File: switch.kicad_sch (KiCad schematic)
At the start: 4 parts, among them U10 74LVC1G3157, U11 74LVC1G3157, U12 74LVC1G3157, U9 74LVC1G3157

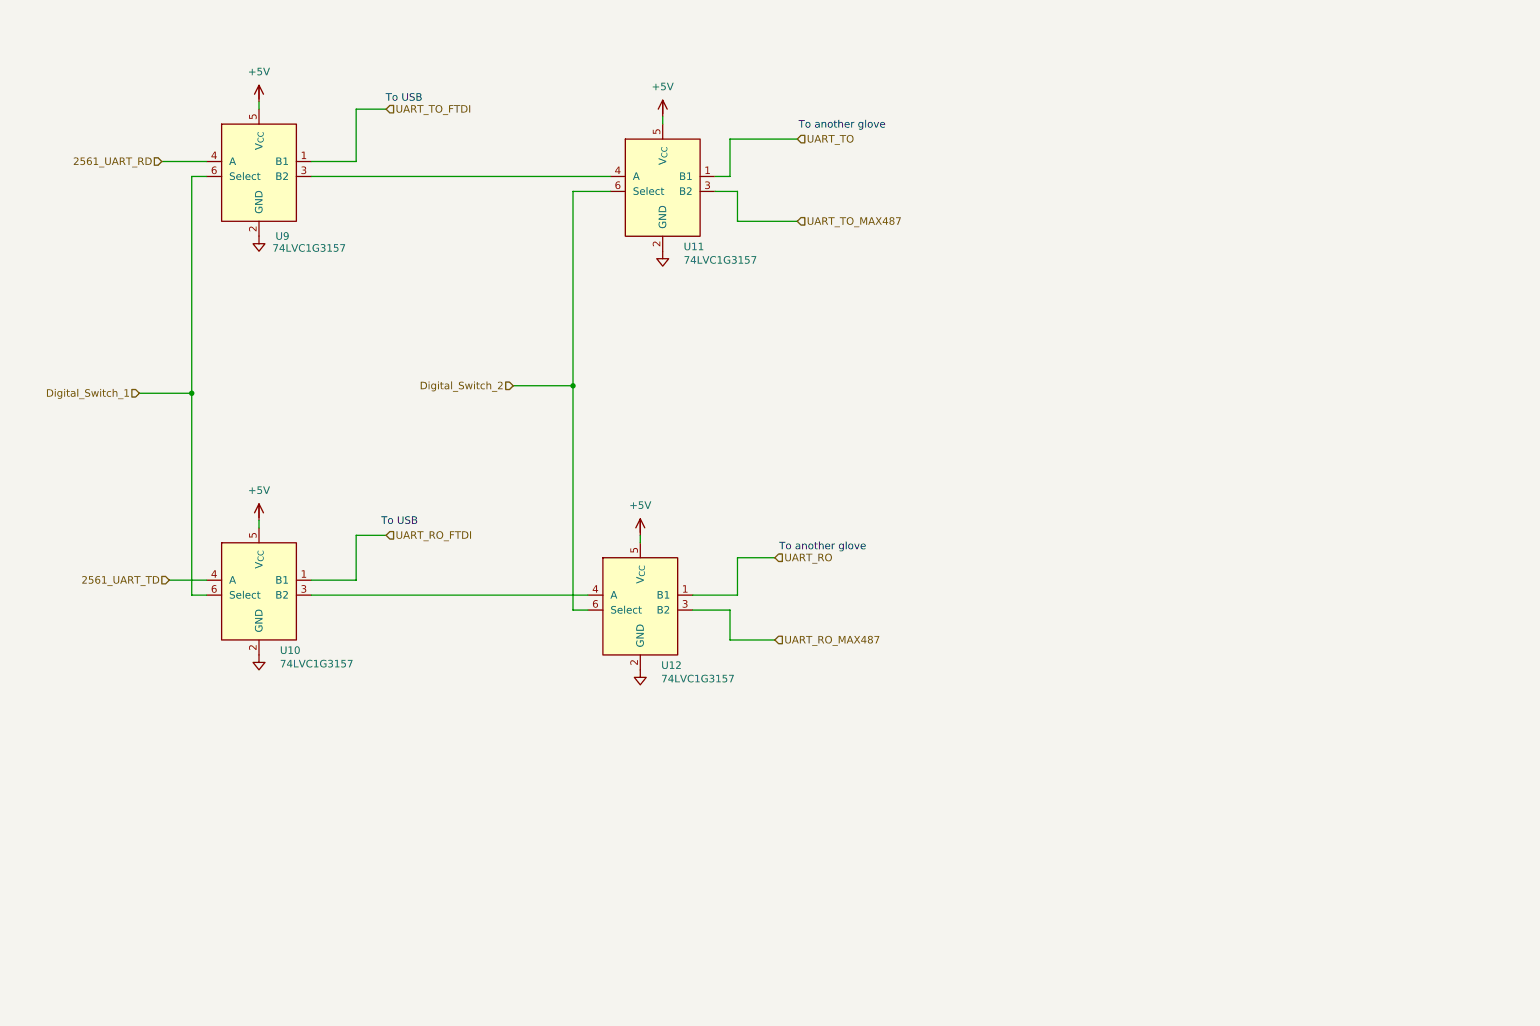
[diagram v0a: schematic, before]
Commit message: add USB conn (ongoing)
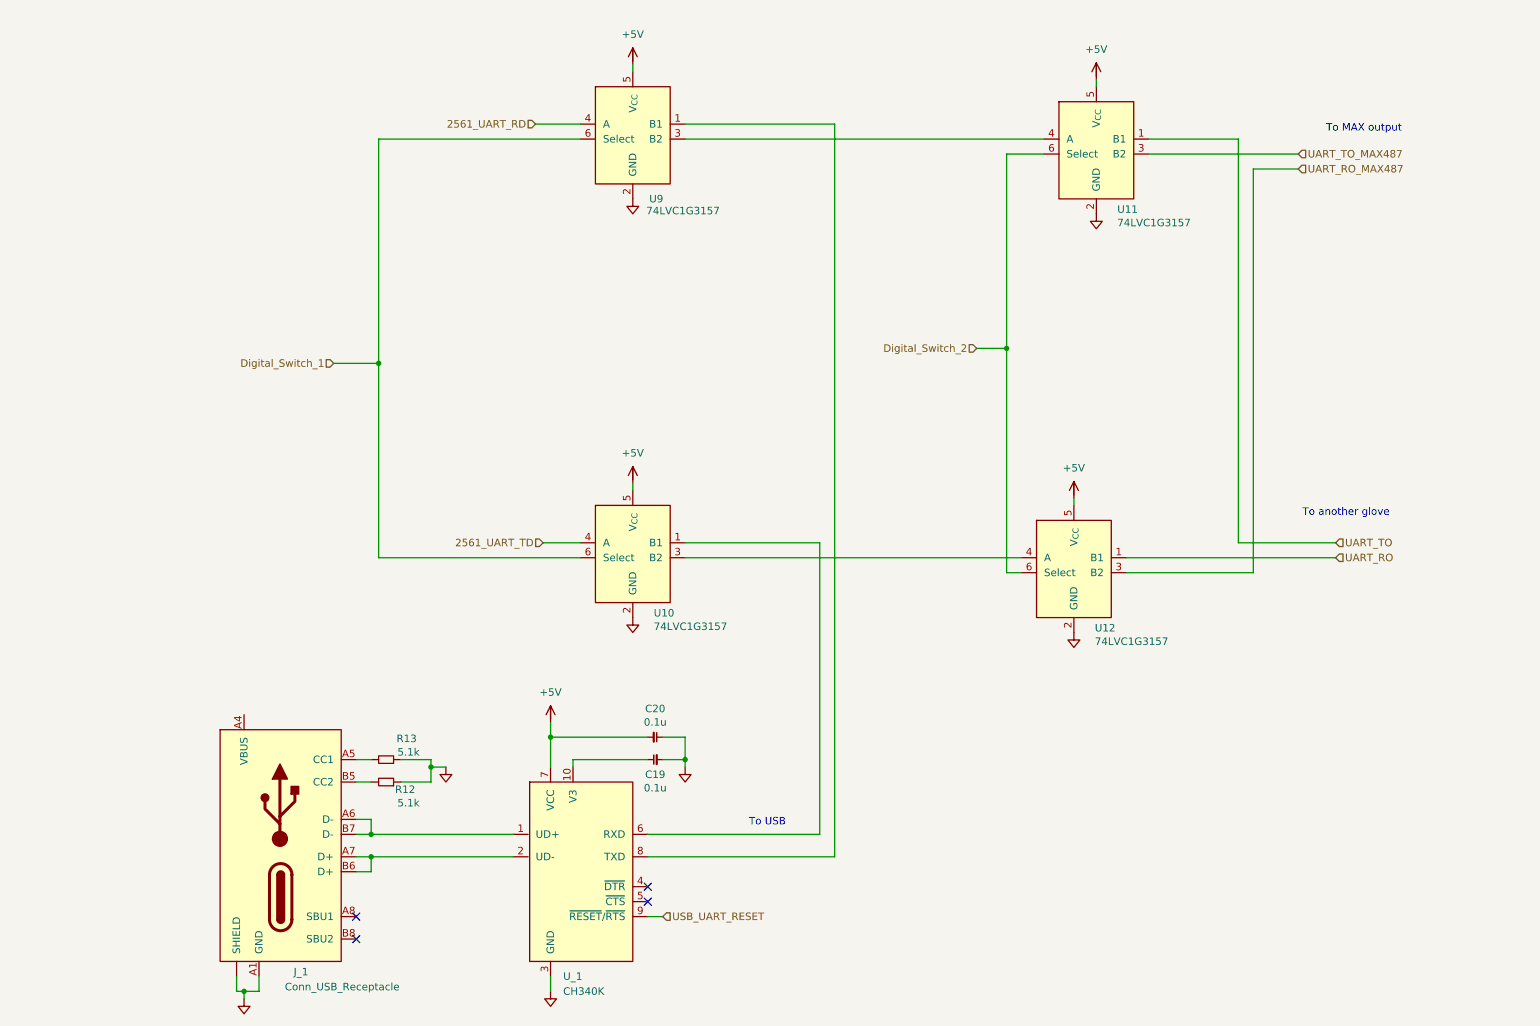
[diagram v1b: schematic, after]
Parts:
- added C19, C20: 0.1u, symbol G-Love:C
- added J_1: Conn_USB_Receptacle, symbol G-Love:J_USB_RECEPTACLE
- added R12, R13: 5.1k, symbol G-Love:R
- added U_1: CH340K, symbol G-Love:CH340K
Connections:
- net +5V: now also C20.1, U_1.7 (VCC)
- net GND: now also C19.1, C20.2, J_1. (SHIELD), J_1.A1 (GND), J_1.A12 (GND), J_1.B1 (GND), J_1.B12 (GND), R12.1, R13.1, U_1.0 (GND), U_1.3 (GND)
- net UART_RO_FTDI: no longer names the net of U10.1 (B1)
- net UART_RO_FTDI: now also U_1.6 (RXD)
- net UART_TO_FTDI: no longer names the net of U9.1 (B1)
- net UART_TO_FTDI: now also U_1.8 (TXD)
- new net: C19.2, U_1.10 (V3)
- new net: J_1.A5 (CC1), R13.2
- new net: J_1.A6 (D-), J_1.B7 (D-), U_1.1 (UD+)
- new net: J_1.A7 (D+), J_1.B6 (D+), U_1.2 (UD-)
- new net: J_1.B5 (CC2), R12.2
- new net USB_UART_RESET: U_1.9 (~{RESET}/~{RTS})
- new net VBUS: J_1.A4 (VBUS), J_1.A9 (VBUS), J_1.B4 (VBUS), J_1.B9 (VBUS)
- no-connect marks 0 -> 4
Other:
- note added: "To MAX output"
- moved on the sheet: U10, U11, U12, U9

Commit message: group by theme in hierarchical subsheets
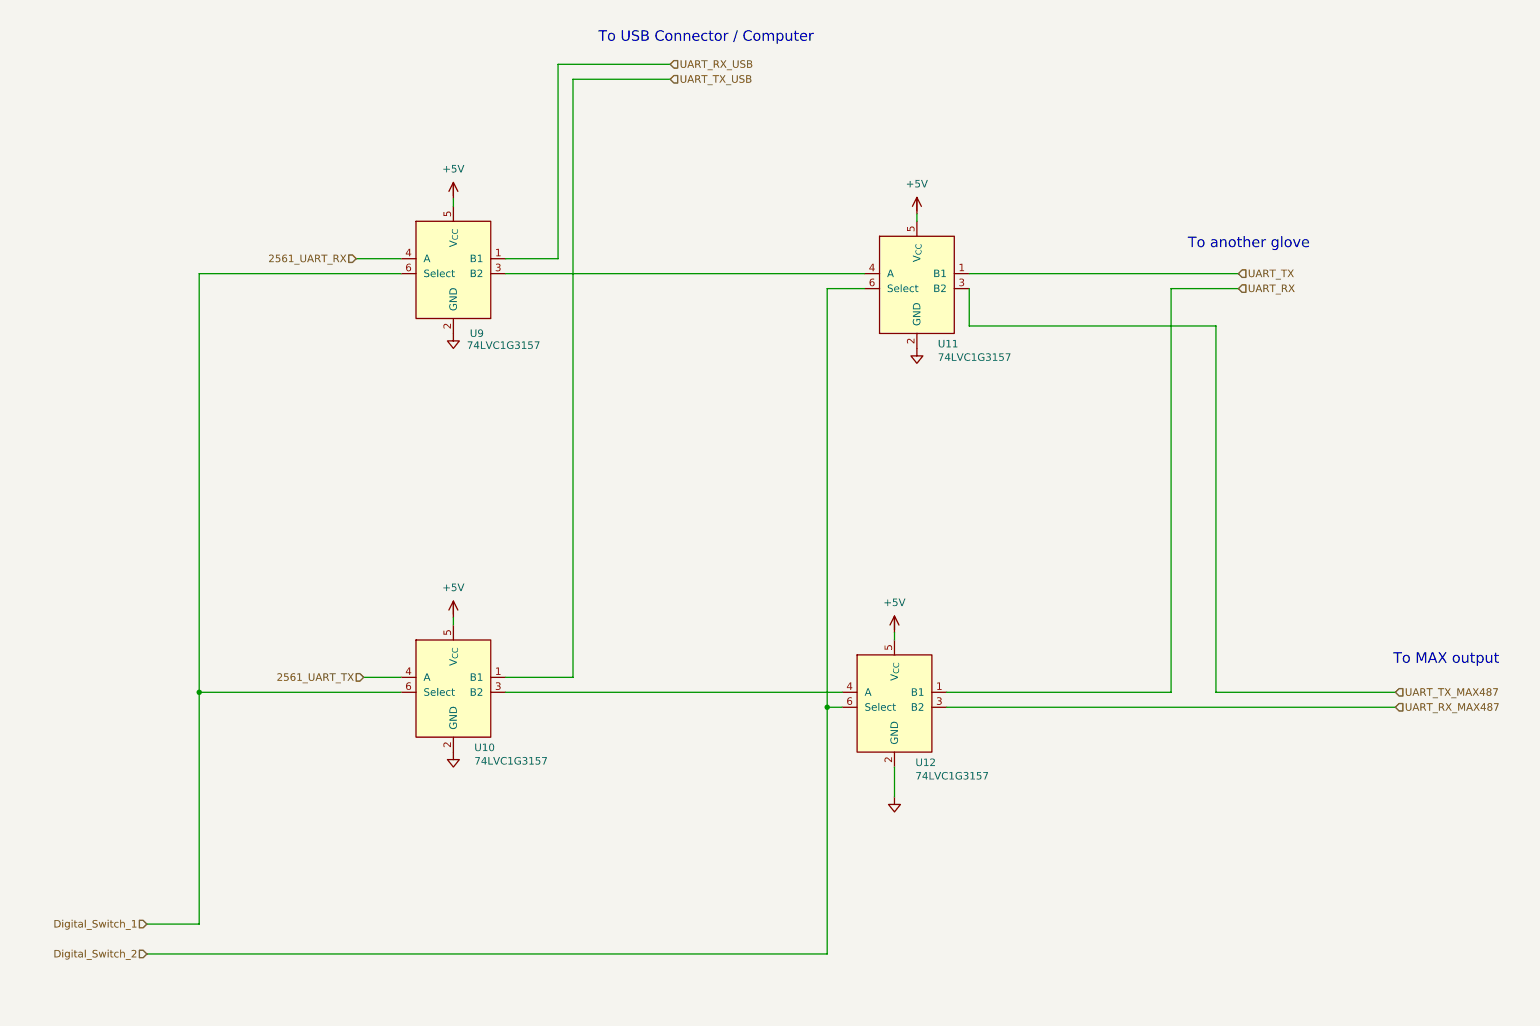
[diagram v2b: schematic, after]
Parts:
- removed C19, C20: 0.1u, symbol G-Love:C
- removed J_1: Conn_USB_Receptacle, symbol G-Love:J_USB_RECEPTACLE
- removed R12, R13: 5.1k, symbol G-Love:R
- removed U_1: CH340K, symbol G-Love:CH340K
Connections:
- net UART_RX_USB: now reaches U9.1 (B1)
- net UART_TX_USB: now reaches U10.1 (B1)
- net 2561_UART_RD renamed 2561_UART_RX
- net 2561_UART_TD renamed 2561_UART_TX
- net UART_RO renamed UART_RX
- net UART_RO_MAX487 renamed UART_RX_MAX487
- net UART_TO renamed UART_TX
- net UART_TO_MAX487 renamed UART_TX_MAX487
- no-connect marks 4 -> 0
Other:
- note added: "To USB Connector / Computer"
- note removed: "To USB"
- moved on the sheet: U10, U11, U12, U9

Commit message: finish
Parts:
- added flow13, flow14, flow15, flow16, flow17, flow18, flow19, flow20, flow21, flow22, flow23, flow24, flow25, flow26, flow27, flow28, flow29, flow30: (no value), symbol G-Love:FlowDirection
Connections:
- net UART_RX: now also U11.1 (B1); no longer U12.1 (B1)
- net UART_RX_MAX487: now also U11.3 (B2); no longer U12.3 (B2)
- net UART_TX: now also U12.1 (B1); no longer U11.1 (B1)
- net UART_TX_MAX487: now also U12.3 (B2); no longer U11.3 (B2)

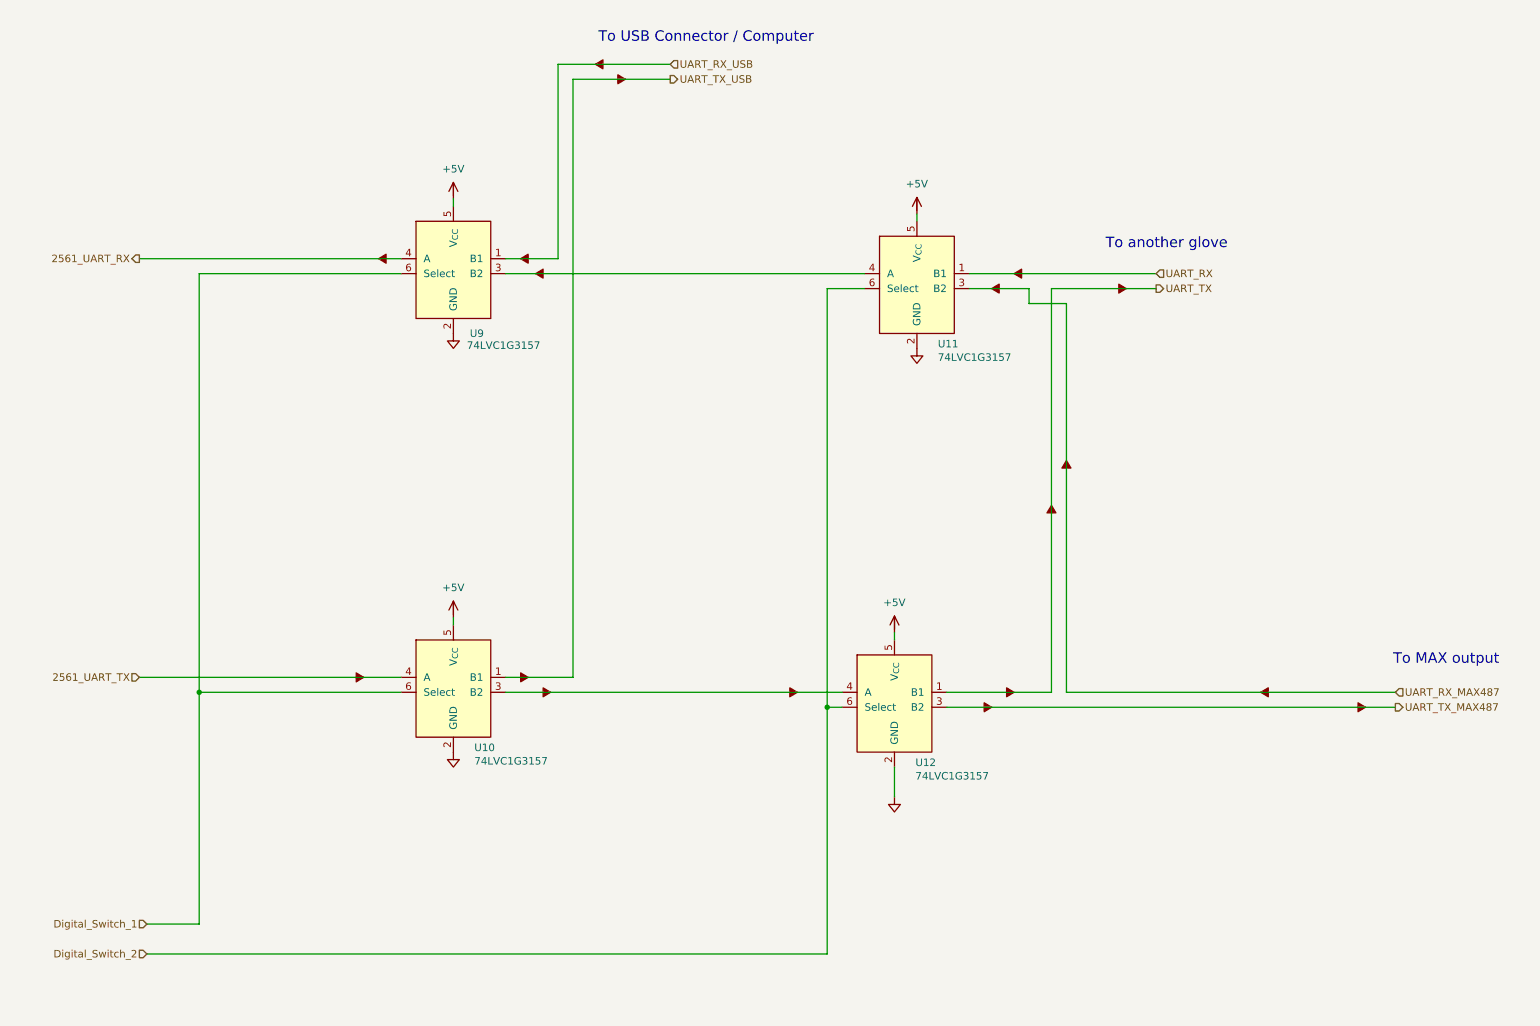
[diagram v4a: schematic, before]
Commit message: Je crois que j'ai fini, je fais l'erc demain en revoyant la logique des switch, notamment les selections avec transistors
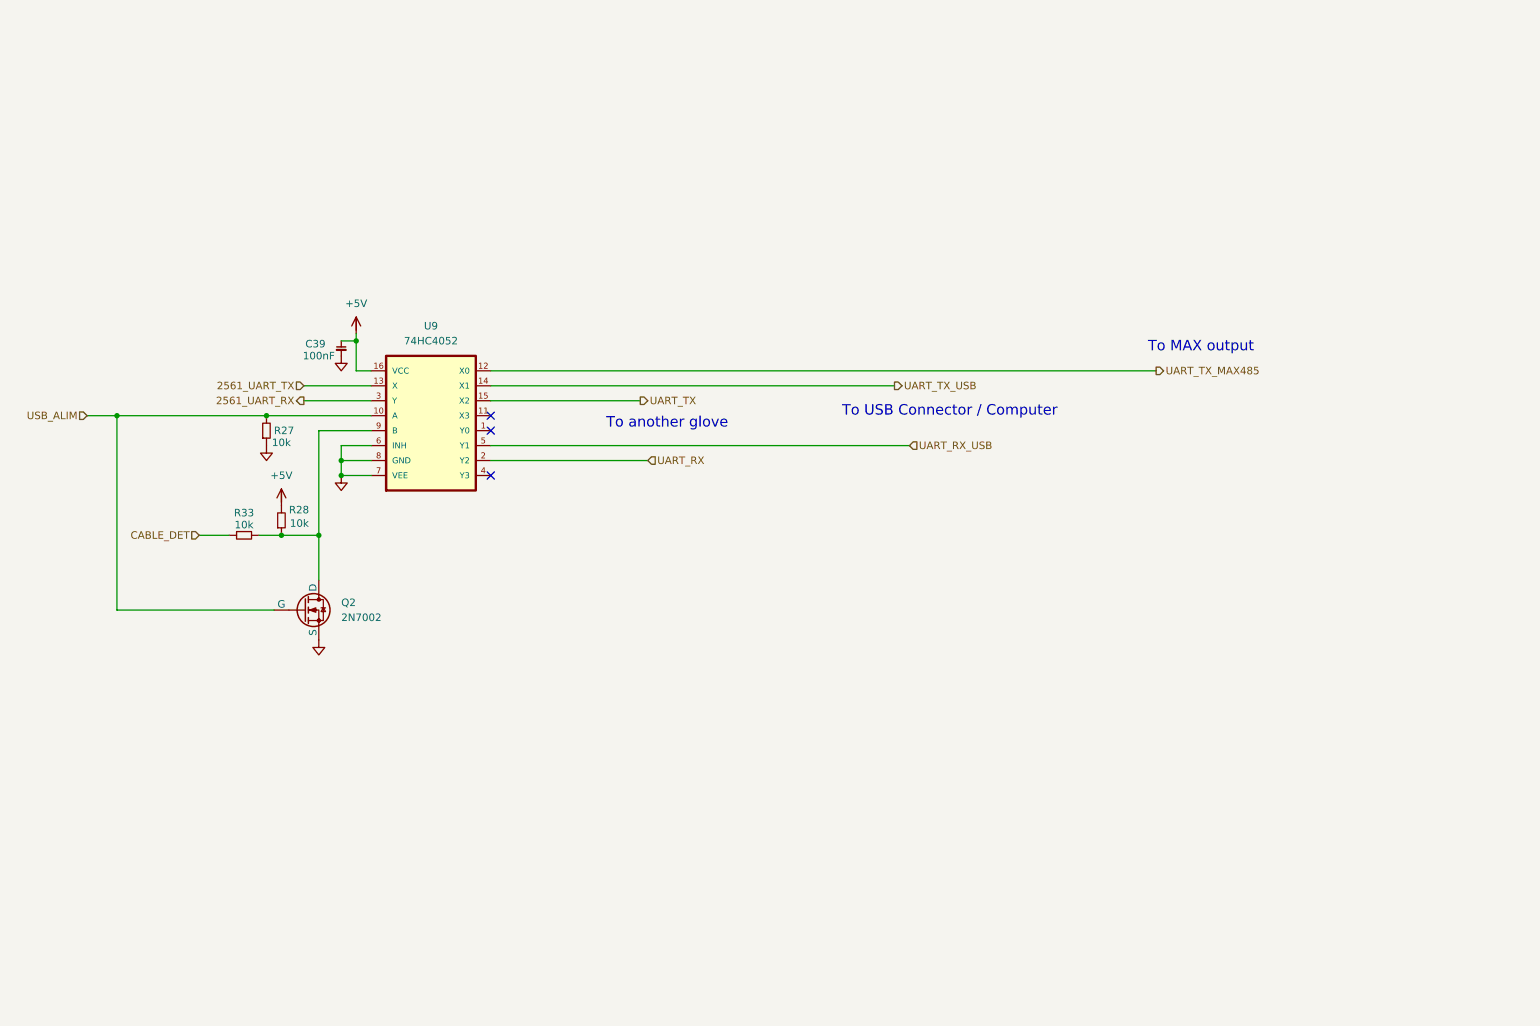
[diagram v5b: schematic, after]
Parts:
- removed U10, U11, U12, U9: 74LVC1G3157, symbol G-Love:74LVC1G3157
- removed flow13, flow14, flow15, flow16, flow17, flow18, flow19, flow20, flow21, flow22, flow23, flow24, flow25, flow26, flow27, flow28, flow29, flow30: (no value), symbol G-Love:FlowDirection
- added C39: 100nF, symbol G-Love:C
- added Q2: 2N7002, Package_TO_SOT_SMD:SOT-23, symbol Transistor_FET:2N7002
- added R27, R28, R33: 10k, symbol G-Love:R
- added U9: 74HC4052, symbol G-Love:74HC4052
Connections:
- net +5V: now also C39.2, R28.2, U9.16 (VCC)
- net 2561_UART_RX: now also U9.3 (Y)
- net 2561_UART_TX: now also U9.13 (X)
- net GND: now also C39.1, Q2.2 (S), R27.1, U9.6 (INH), U9.7 (VEE), U9.8 (GND)
- net UART_RX: now also U9.2 (Y2)
- net UART_RX_USB: now also U9.5 (Y1)
- net UART_TX: now also U9.15 (X2)
- net UART_TX_USB: now also U9.14 (X1)
- new net: Q2.3 (D), R28.1, R33.2, U9.9 (B)
- new net CABLE_DET: R33.1
- new net UART_TX_MAX485: U9.12 (X0)
- new net USB_ALIM: Q2.1 (G), R27.2, U9.10 (A)
- no-connect marks 0 -> 3

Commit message: version final V1
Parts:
- removed C39: 100nF, symbol G-Love:C
- removed Q2: 2N7002, Package_TO_SOT_SMD:SOT-23, symbol Transistor_FET:2N7002
- removed R27, R28, R33: 10k, symbol G-Love:R
- removed U9: 74HC4052, symbol G-Love:74HC4052
- added C19, C20, C26, C27: 100nF, symbol G-Love:C
- added U10, U11: 74HC4052, symbol G-Love:74HC4052
- added U_1: CH340K, symbol G-Love:CH340K
- added flow10, flow11, flow12, flow13, flow14, flow15, flow16, flow33, flow34, flow9: (no value), symbol G-Love:FlowDirection
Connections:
- net +5V: now also C19.1, C20.1, C20.2, C26.1, C26.2, C27.1, C27.2, U10.16 (VCC), U10.6 (INH), U10.7 (VEE), U10.8 (GND), U11.16 (VCC), U11.6 (INH), U11.7 (VEE), U11.8 (GND), U11.9 (B), U_1.0 (GND), U_1.3 (GND), U_1.7 (VCC)
- net 2561_UART_RX: now also U10.3 (Y)
- net 2561_UART_TX: now also U10.13 (X)
- new net: C19.2, U_1.10 (V3)
- new net: U10.12 (X0), U_1.6 (RXD)
- new net: U10.14 (X1), U11.13 (X)
- new net: U10.5 (Y1), U11.3 (Y)
- new net CH340_UART_DTR: U10.1 (Y0), U_1.4 (~{DTR}), U_1.8 (TXD)
- new net DMX/TX_DMX: U10.15 (X2)
- new net SBU1: U11.12 (X0), U11.5 (Y1)
- new net SBU2: U11.1 (Y0), U11.14 (X1)
- new net UART_MUX_SEL_A: U10.10 (A)
- new net UART_MUX_SEL_B: U10.9 (B)
- new net UD+: U_1.1 (UD+)
- new net UD-: U_1.2 (UD-)
- new net USB_SELECT: U11.10 (A)
- no-connect marks 3 -> 9
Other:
- added sheet DMX (dmx.kicad_sch)
- note added: "CH340K - Bridge UART to D+/D- Clock is included on the K chip Circuit setup based on 7.8 of datasheet DTR = Data Terminal Ready may be needed for flashing code CTS = Clear To Send, buffer full uneeded if buffer handled in software"
- note removed: "To MAX output"
- note removed: "To USB Connector / Computer"
- note removed: "To another glove"

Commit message: add: bom
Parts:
- C19, C20, C26, C27: Price (none) -> 1.44/100; SUPPLIER (none) -> https://www.lcsc.com/product-detail/C1591.html
- U10, U11: Price None -> 0.73; SUPPLIER (none) -> https://www.lcsc.com/product-detail/C11350.html
- U_1: Price (none) -> 0.6; SUPPLIER (none) -> https://www.lcsc.com/product-detail/C968586.html

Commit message: Ajout led indication
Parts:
- added D101, D102: YELLOW, symbol G-Love:LED_Indicator
- added R23, R27, R28, R30: 1k, symbol G-Love:R
- added flow7, flow8: (no value), symbol G-Love:FlowDirection
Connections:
- net +5V: now also R28.1, R30.1
- net 2561_UART_RX: now also R23.2; no longer U10.3 (Y)
- net 2561_UART_TX: now also D102.2 (K), R27.2; no longer U10.13 (X)
- new net: D102.1 (A), R30.2
- new net: D101.1 (A), R28.2
- new net: D101.2 (K), R23.1, U10.3 (Y)
- new net: R27.1, U10.13 (X)
